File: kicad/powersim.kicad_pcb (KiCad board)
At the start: 2 copper layers, 84.6 x 64 mm, 9 parts, among them J1 Bus_PCI_Express_x1, J2 Conn_01x02_Pin, J6 USB_C_Receptacle_USB2.0_16P, U1 AP63203WU

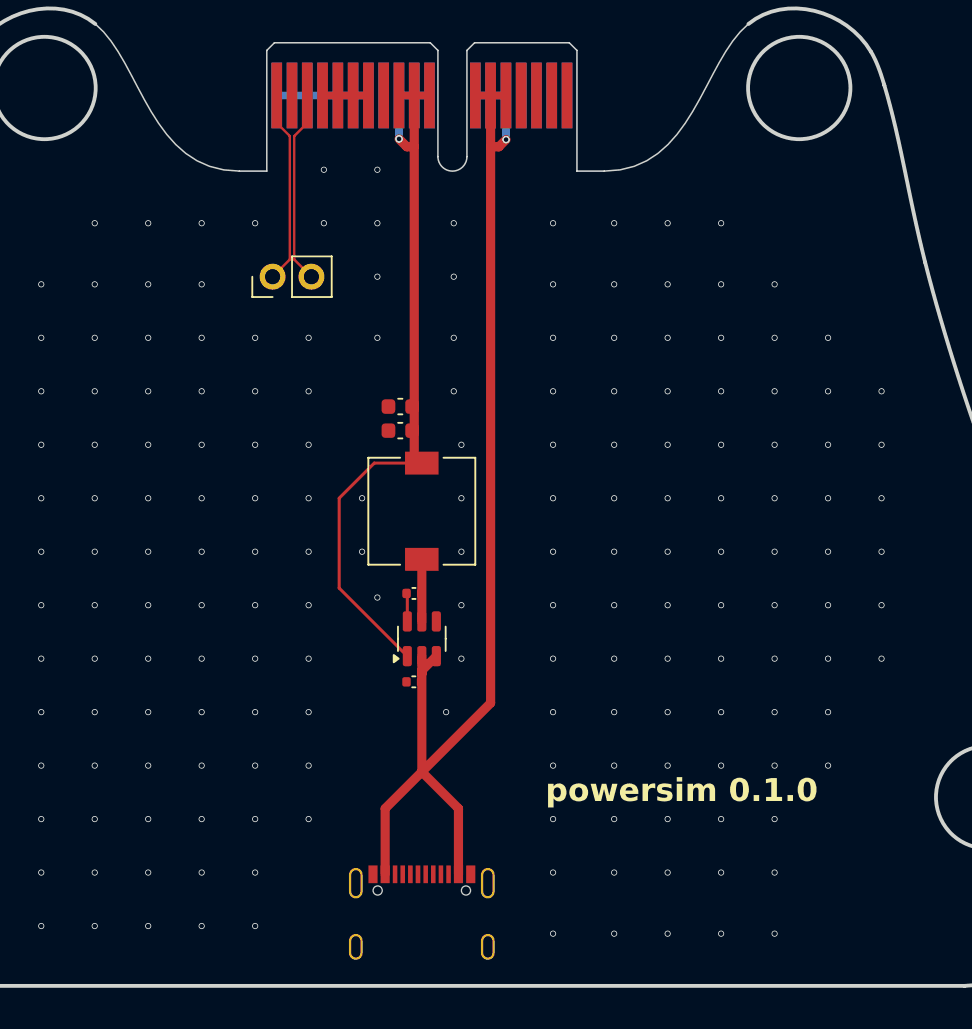
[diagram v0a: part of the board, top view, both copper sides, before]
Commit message: add test points and USB pull down resistors
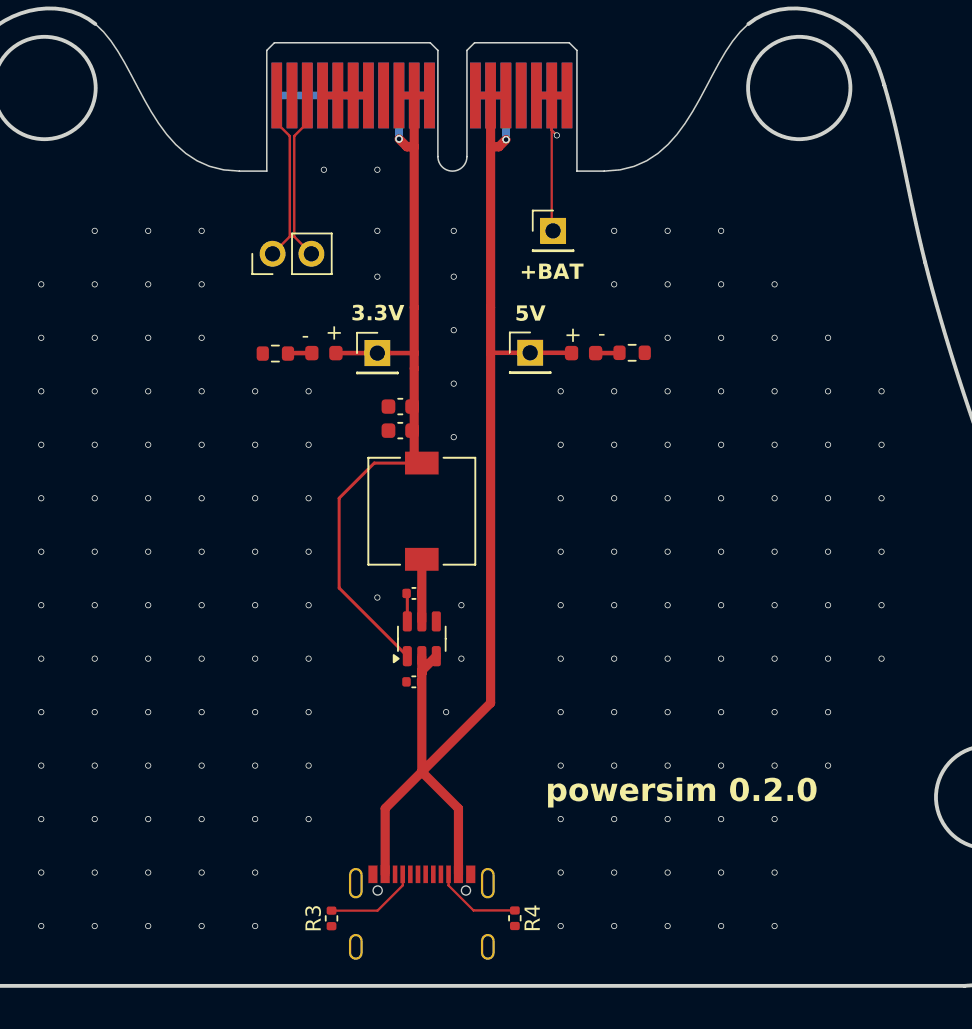
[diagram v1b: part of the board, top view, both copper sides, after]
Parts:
- added D1: LED, LED_SMD:LED_0603_1608Metric, F.Cu at (140.0, 81.0)
- added D2: LED, LED_SMD:LED_0603_1608Metric, F.Cu at (157.0, 81.0)
- added R1: 150, Resistor_SMD:R_0603_1608Metric, F.Cu at (136.8, 81.0)
- added R2: 150, Resistor_SMD:R_0603_1608Metric, F.Cu at (160.2, 81.0)
- added R3: 5.1k, Resistor_SMD:R_0402_1005Metric, F.Cu at (140.5, 118.0)
- added R4: 5.1k, Resistor_SMD:R_0402_1005Metric, F.Cu at (152.5, 118.0)
- added TP1: TestPoint, Connector_PinHeader_2.54mm:PinHeader_1x01_P2.54mm_Vertical, F.Cu at (153.5, 81.0)
- added TP2: TestPoint, Connector_PinHeader_2.54mm:PinHeader_1x01_P2.54mm_Vertical, F.Cu at (143.5, 81.0)
- added TP3: TestPoint, Connector_PinHeader_2.54mm:PinHeader_1x01_P2.54mm_Vertical, F.Cu at (155.0, 73.0)
- moved J2 1.50 mm to (136.6, 74.5)
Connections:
- J1 pad A16: unconnected-(J1-PERp0-PadA16) -> +BAT
- J1 pad A17: unconnected-(J1-PERn0-PadA17) -> +BAT
- J1 pad A18: unconnected-(J1-GND-PadA18) -> +BAT
- J1 pad B16: unconnected-(J1-GND-PadB16) -> +BAT
- J1 pad B17: unconnected-(J1-~{PRSNT2}-PadB17) -> +BAT
- J1 pad B18: unconnected-(J1-GND-PadB18) -> +BAT
- J6 pad A5: unconnected-(J6-CC1-PadA5) -> Net-(J6-CC1)
- J6 pad B5: unconnected-(J6-CC2-PadB5) -> Net-(J6-CC2)
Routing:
- net +BAT: track 0.00 -> 18.4 mm, vias 0 -> 1
- net Net-(J6-CC1): track 0.00 -> 6.07 mm
- net Net-(J6-CC2): track 0.00 -> 5.75 mm
- net +5V: track 78.6 -> 83.9 mm
- net +3.3V: track 50.7 -> 55.6 mm
- net Net-(D1-K): track 0.00 -> 1.57 mm
- net Net-(D2-K): track 0.00 -> 1.57 mm
- net CANP: track 12.7 -> 11.2 mm
- net CANN: track 12.7 -> 11.2 mm
- net GND: vias 194 -> 181
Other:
- board text added: "+BAT"
- board text added: "3.3V"
- board text added: "5V"
- board text added: "powersim 0.2.0"
- board text removed: "powersim 0.1.0"

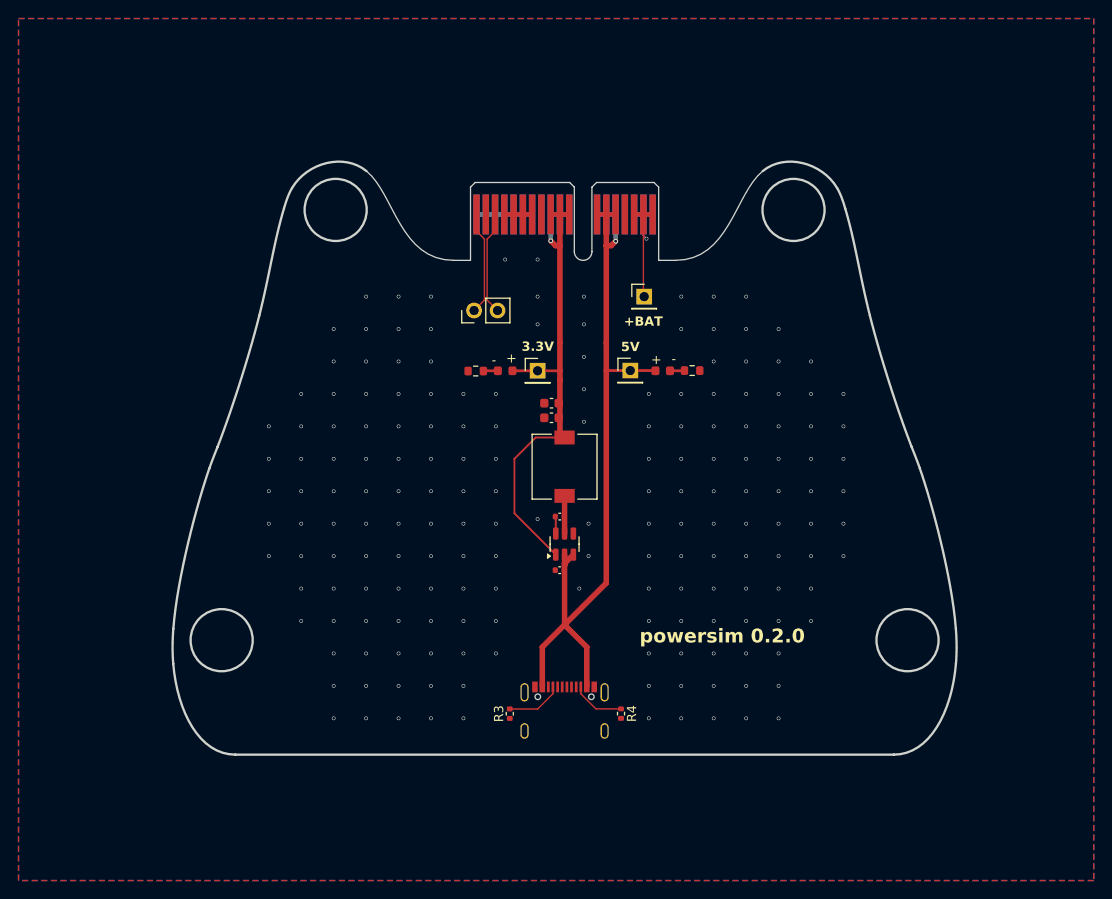
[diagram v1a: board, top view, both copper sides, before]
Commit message: update board outline, delete old production files
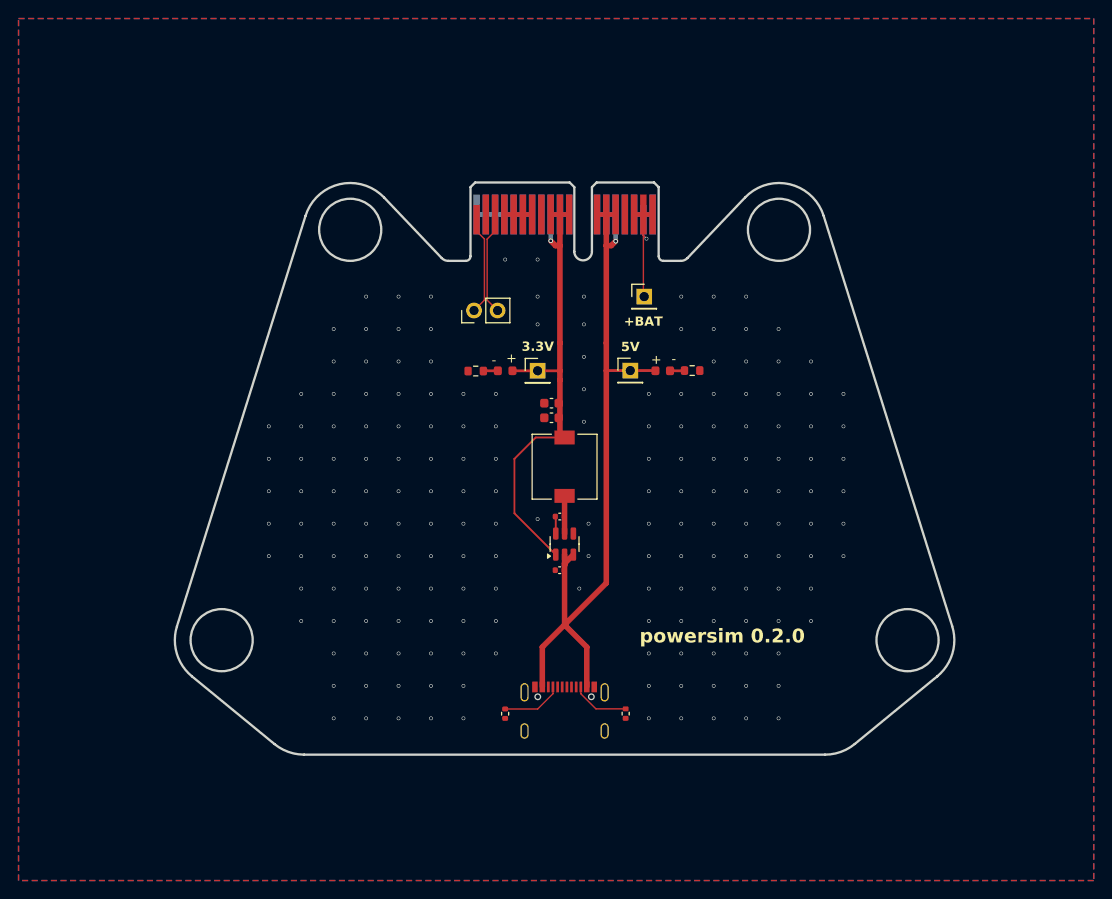
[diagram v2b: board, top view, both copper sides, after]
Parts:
- moved R3 0.50 mm to (140.0, 118.0)
- moved R4 0.50 mm to (153.0, 118.0)
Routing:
- net Net-(J6-CC2): track 5.75 -> 6.25 mm
- net Net-(J6-CC1): track 6.07 -> 6.57 mm
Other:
- board size 84.6 x 64 mm -> 84.1 x 61.7 mm

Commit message: finalize board, update production files
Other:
- board text added: "+VBAT"
- board text added: "H"
- board text added: "L"
- board text removed: "+BAT"
